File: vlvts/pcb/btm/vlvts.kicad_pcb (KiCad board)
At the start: 2 copper layers, 45 x 45 mm, 30 parts, among them J3 Conn_01x14_Female, J5 Conn_ARM_JTAG_SWD_10, M1 Motor_DC_ALT, U1 XC9110A, U2 XC9111C, U3 XC9111C, U4 DRV8210, U6 Holyiot-18010

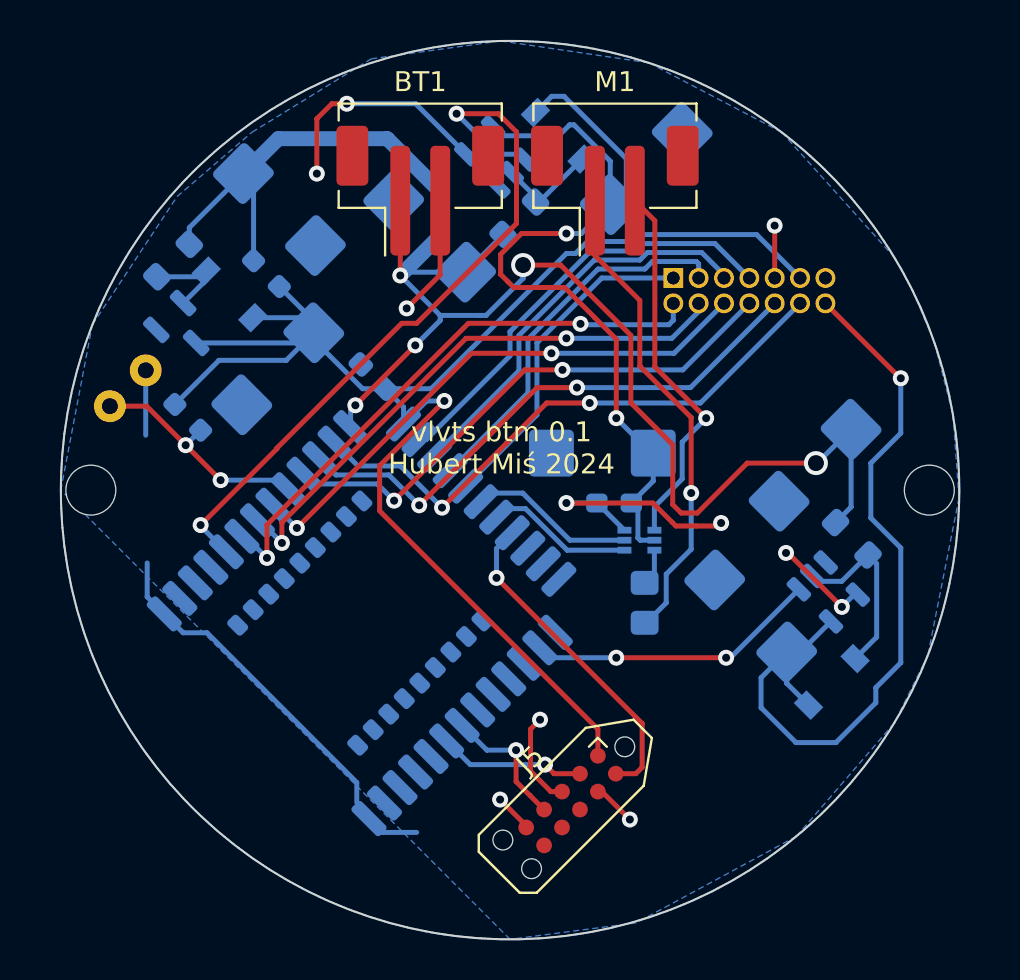
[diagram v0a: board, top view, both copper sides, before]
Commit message: vlvts: partial updates to PCBs
Fixing problems spotted after the manufacturing of an initial batch
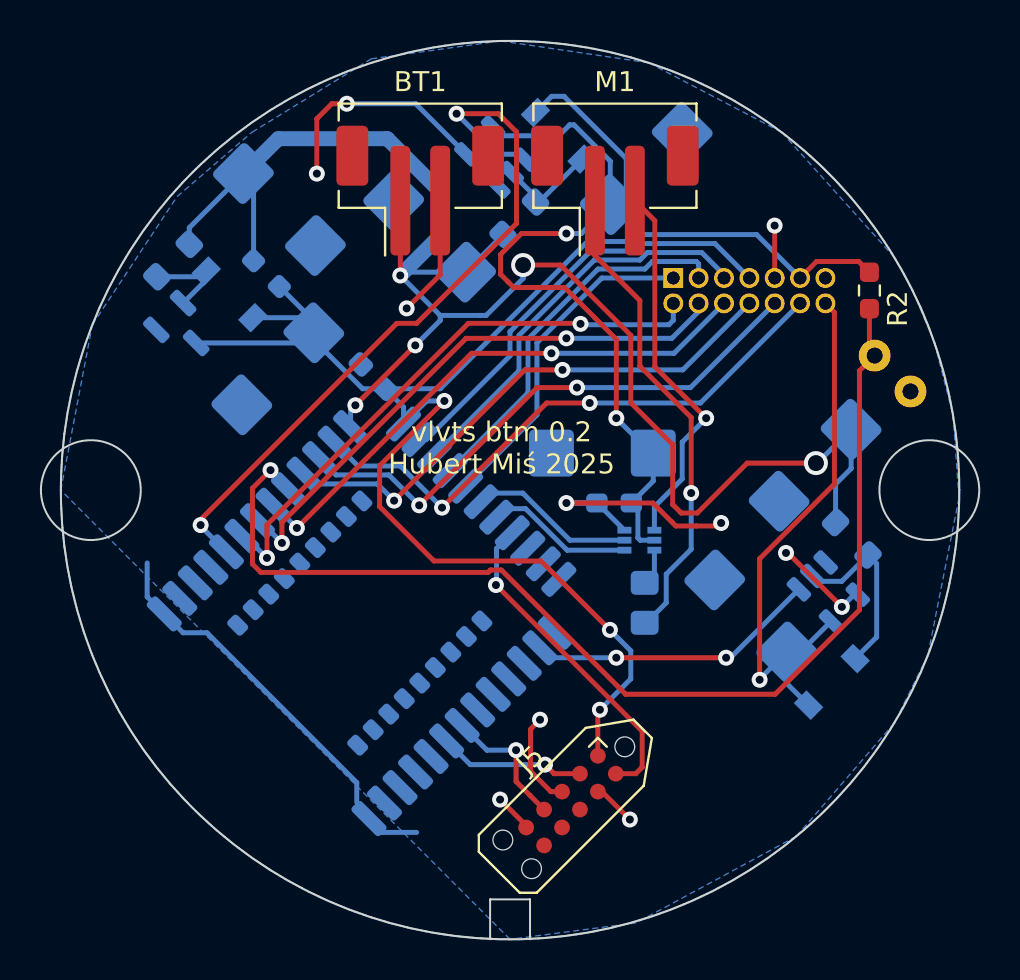
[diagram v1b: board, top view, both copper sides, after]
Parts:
- removed H3, H4: MountingHole, MountingHole:MountingHole_2.5mm
- R2: moved to F.Cu
- moved TH1 38.4 mm to (97.3, 93.3), turned to -45 degrees
- moved R2 34.7 mm to (97.0, 90.0), turned to -90 degrees
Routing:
- net TEMP: track 11.7 -> 57.6 mm, vias 2 -> 1
- net VEE: track 39.9 -> 28.5 mm
- net GND: track 68.9 -> 65.7 mm
- net VDD: track 76.7 -> 76.8 mm, vias 1 -> 3
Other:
- board size 45 x 45 mm -> 47 x 45 mm
- board text added: "vlvts btm 0.2 Hubert Miś 2025"
- board text removed: "vlvts btm 0.1 Hubert Miś 2024"

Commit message: vlvts: new pcb
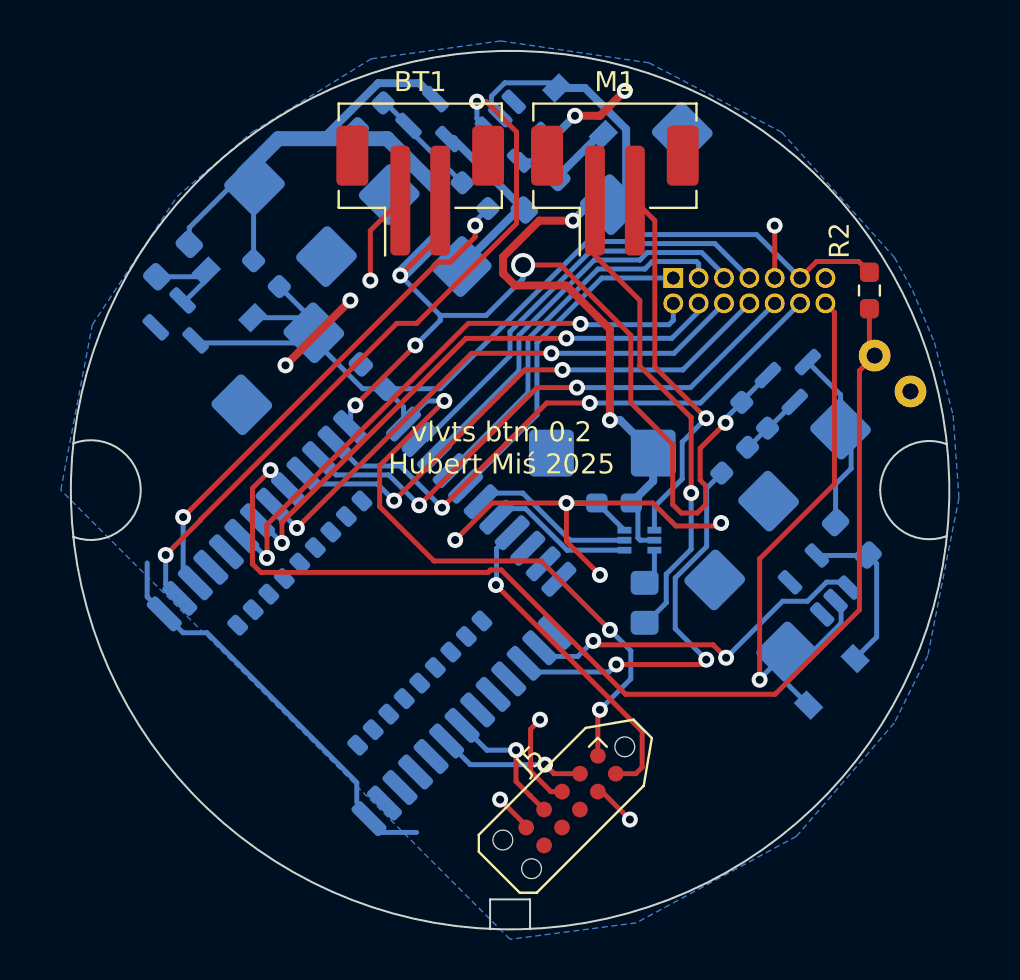
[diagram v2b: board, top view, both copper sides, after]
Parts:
- added Q1: YJL2305A-YAN, Package_TO_SOT_SMD:SOT-23, B.Cu at (75.2, 81.8)
- added Q2: YJL2305A-YAN, Package_TO_SOT_SMD:SOT-23, B.Cu at (93.2, 94.2)
- added R3: 100, Resistor_SMD:R_0603_1608Metric_Pad0.98x0.95mm_HandSolder, B.Cu at (77.2, 85.2)
- added R4: 10k, Resistor_SMD:R_0603_1608Metric_Pad0.98x0.95mm_HandSolder, B.Cu at (72.0, 81.2)
- added R5: 100, Resistor_SMD:R_0603_1608Metric_Pad0.98x0.95mm_HandSolder, B.Cu at (90.2, 98.5)
- added R7: 10k, Resistor_SMD:R_0603_1608Metric_Pad0.98x0.95mm_HandSolder, B.Cu at (91.2, 96.2)
- U2, U3: value XC9111C -> XC9110C
- moved C5 22.8 mm to (74.8, 87.0), turned to 135 degrees
- moved C2 22.0 mm to (93.8, 98.8), turned to -135 degrees
- moved U3 1.65 mm to (79.3, 82.0), turned to -45 degrees
- moved D44 1.62 mm to (82.5, 81.0)
- moved L3 1.62 mm to (80.5, 85.2)
- moved C1 0.78 mm to (68.0, 86.5)
- moved U2 0.56 mm to (94.5, 104.8), turned to 135 degrees
- moved U1 0.13 mm to (62.6, 91.8)
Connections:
- net BTN_C renamed CAP_DATA
- net BTN_L renamed CAP_CLK
- net BTN_R renamed CAP_IRQ
- BT1 pad 1: BATT_V -> GND
- BT1 pad 2: GND -> BATT_V
- C2 pad 1: BATT_V -> Net-(Q2-D)
- C5 pad 1: BATT_V -> Net-(Q1-D)
- L2 pad 1: BATT_V -> Net-(Q2-D)
- L3 pad 1: BATT_V -> Net-(Q1-D)
- U2 pad 1: LED_PWR -> LED_SUP
- U2 pad 2: Net-(D43-A) -> VEE
- U2 pad 5: VEE -> Net-(D43-A)
- U3 pad 1: MOT_PWR -> MOT_SUP
- U3 pad 2: Net-(D44-A) -> VCC
- U3 pad 5: VCC -> Net-(D44-A)
- U6 pad 2: unconnected-(U6-P1.11-Pad2) -> MOT_SUP
- U6 pad 26: LED_PWR -> LED_SUP
- U6 pad 27: unconnected-(U6-TRACEDATA0/P1.00-Pad27) -> LED_PWR
- U6 pad 3: unconnected-(U6-P1.10-Pad3) -> MOT_PWR
- U6 pad 5: MOT_PWR -> unconnected-(U6-P1.15-Pad5)
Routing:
- net MOT_SUP: track 0.00 -> 35.7 mm, vias 0 -> 2
- net LED_SUP: track 0.00 -> 18.9 mm, vias 0 -> 2
- net MOT_PWR: track 36.5 -> 25.7 mm
- net Net-(Q1-D): track 0.00 -> 9.63 mm
- net Net-(Q2-D): track 0.00 -> 9.04 mm
- net LED_PWR: track 14.6 -> 20.5 mm
- net VCC: track 44.9 -> 39.2 mm
- net Net-(Q1-G): track 0.00 -> 5.71 mm
- net Net-(Q2-G): track 0.00 -> 3.30 mm
- net BATT_V: track 83.6 -> 80.5 mm
- net VEE: track 28.5 -> 30.9 mm
- net GND: track 65.7 -> 67.7 mm, vias 11 -> 13
- net Net-(D43-A): track 9.26 -> 8.38 mm
- net Net-(D44-A): track 5.16 -> 5.67 mm
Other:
- board size 47 x 45 mm -> 44 x 44 mm
